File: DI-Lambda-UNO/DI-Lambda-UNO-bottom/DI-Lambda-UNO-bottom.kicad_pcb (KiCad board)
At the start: 2 copper layers, 38.2 x 128.1 mm, 49 parts, among them J10 CONN_02X05, J11 CONN_02X05, J15 CONN_01X06, J16 CONN_01X06, J17 CONN_02X03, J18 USB_OTG, J2 Conn_01X01, J3 CONN_02X05, J4 Conn_01X01, J6 CONN_02X05, J7 CONN_02X04, J8 CONN_02X04, Q1 AO3400, SW1 RESET, U2 USBLC6-2SC6, U3 ATMEGA32U4-MU, U4 3.3v LDO, U5 AP3032, Y1 8Mhz

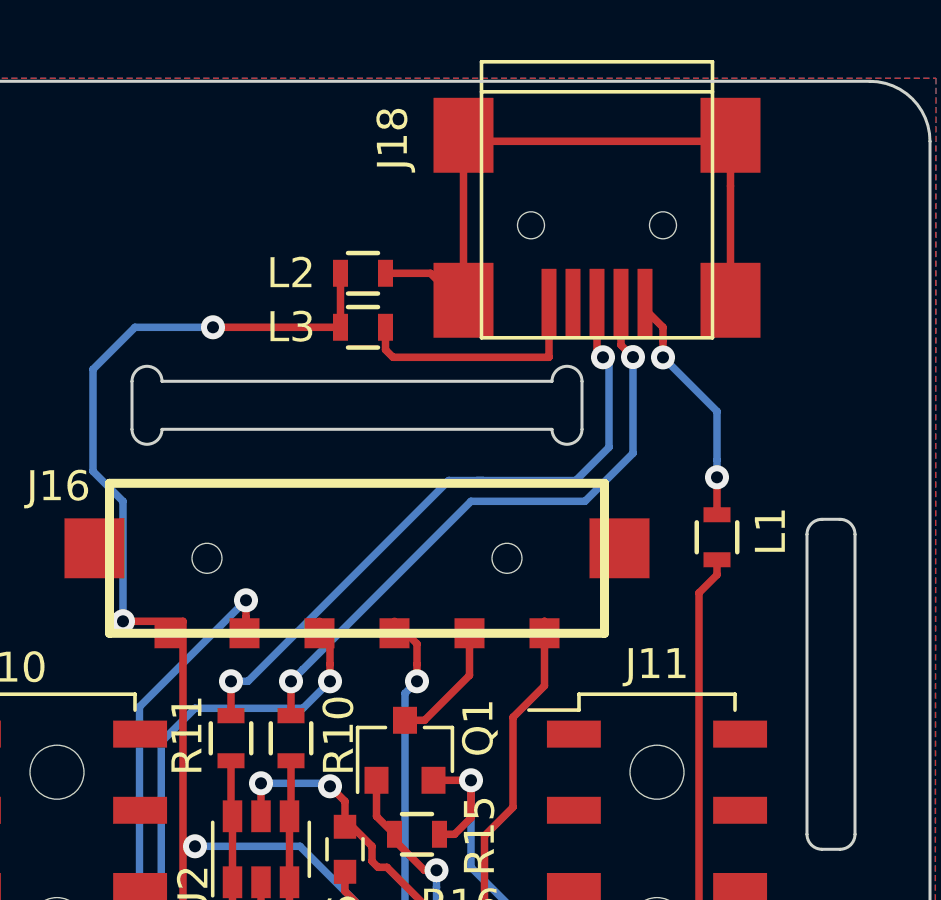
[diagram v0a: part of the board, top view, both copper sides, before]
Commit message: Use Micro-USB instead on Mini on the bottom plate
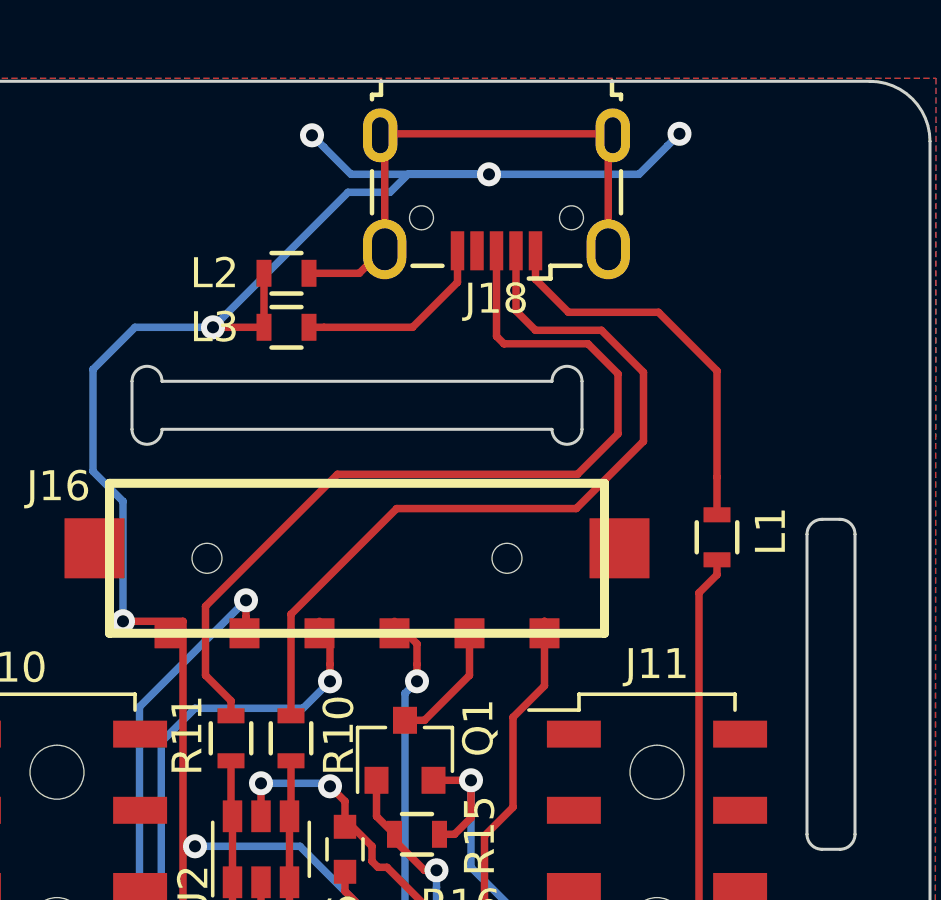
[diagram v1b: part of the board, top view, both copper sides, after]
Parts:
- J18: footprint Connectors:USB_Mini-B -> Connectors_USB:USB_Micro-B_Wuerth-629105150521
- moved J18 3.46 mm to (155.0, 39.8), turned to 180 degrees
- moved L2 2.55 mm to (148.0, 42.5)
- moved L3 2.55 mm to (148.0, 44.3)
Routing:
- net GND: track 196.8 -> 218.9 mm, vias 24 -> 27
- net Net-(J18-Pad3): track 22.1 -> 29.6 mm, vias 2 -> 0
- net Net-(J18-Pad2): track 20.9 -> 27.0 mm, vias 2 -> 0
- net Net-(J18-Pad1): track 7.84 -> 13.1 mm, vias 2 -> 0
- net Net-(J18-Pad6): track 23.0 -> 18.4 mm
- net Net-(J18-Pad5): track 7.90 -> 6.67 mm

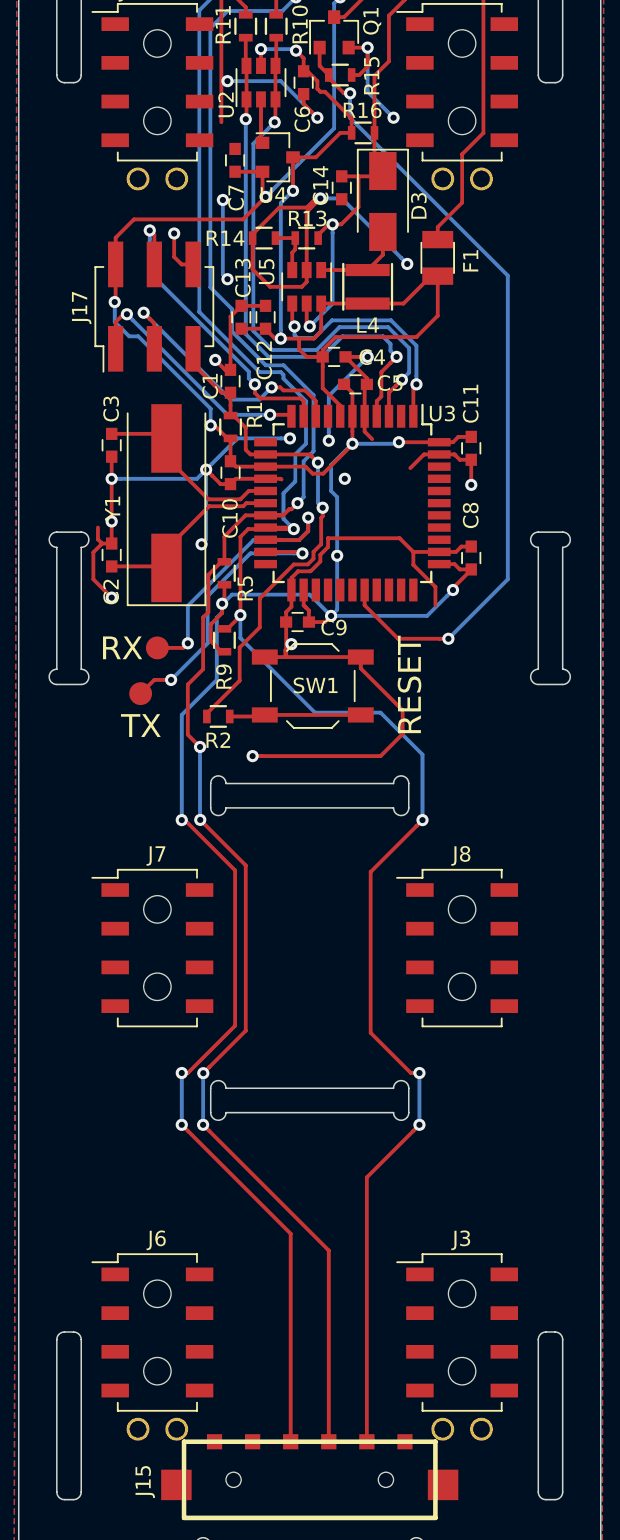
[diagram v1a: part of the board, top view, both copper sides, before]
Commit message: Change pinhole tab length to 15mm
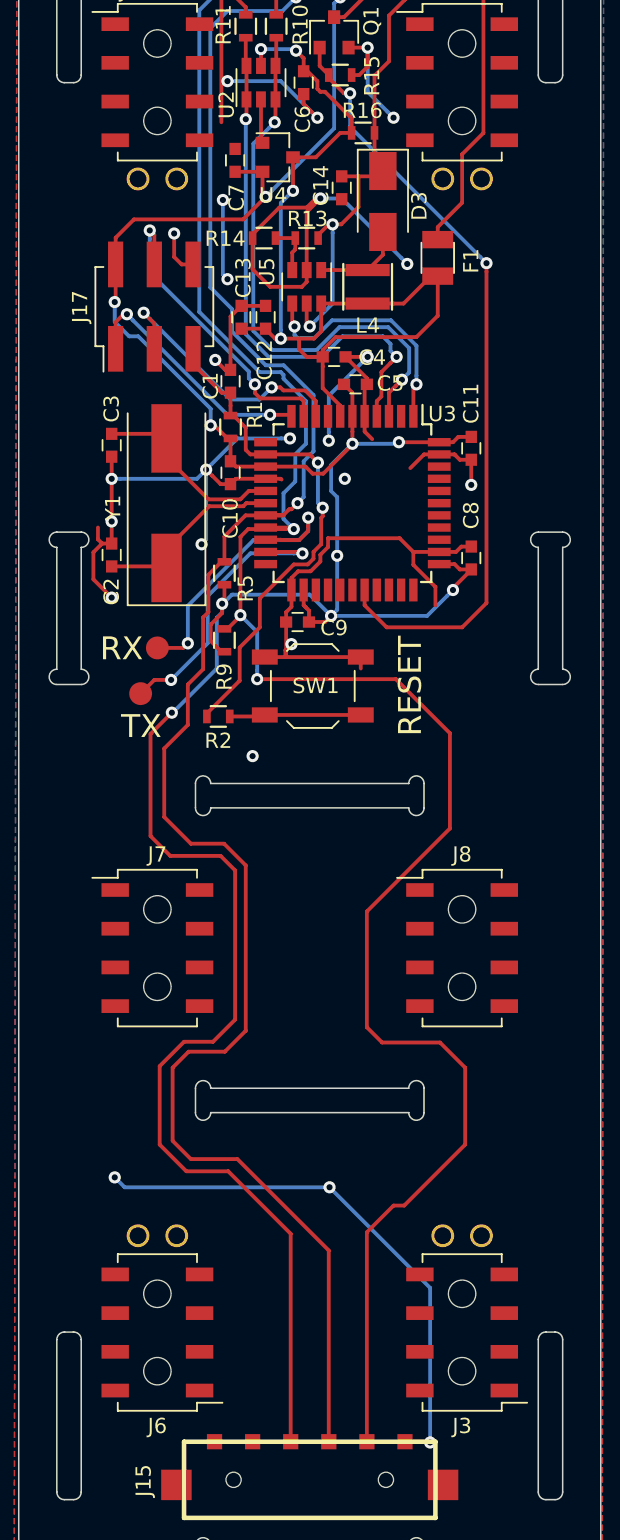
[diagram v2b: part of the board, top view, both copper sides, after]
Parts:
- turned J3 to 180 degrees
- turned J6 to 180 degrees
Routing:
- net GND: track 218.9 -> 238.5 mm, vias 27 -> 30
- net /SDA: track 123.1 -> 132.4 mm, vias 6 -> 4
- net /VCC: track 176.6 -> 183.8 mm, vias 13 -> 11
- net /SCL: track 117.7 -> 124.8 mm, vias 6 -> 2
- net /LED_PWM: track 53.2 -> 51.5 mm
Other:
- outline, holes or cut-outs redrawn

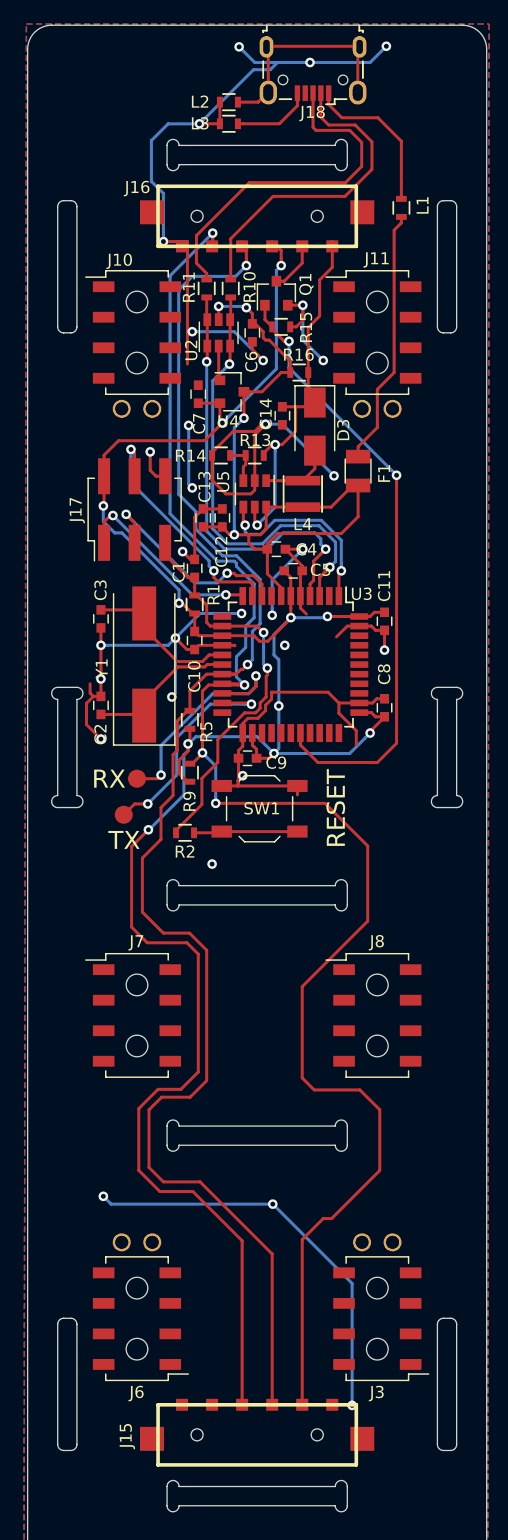
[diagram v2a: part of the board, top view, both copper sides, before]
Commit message: Update schematics to version 1.3
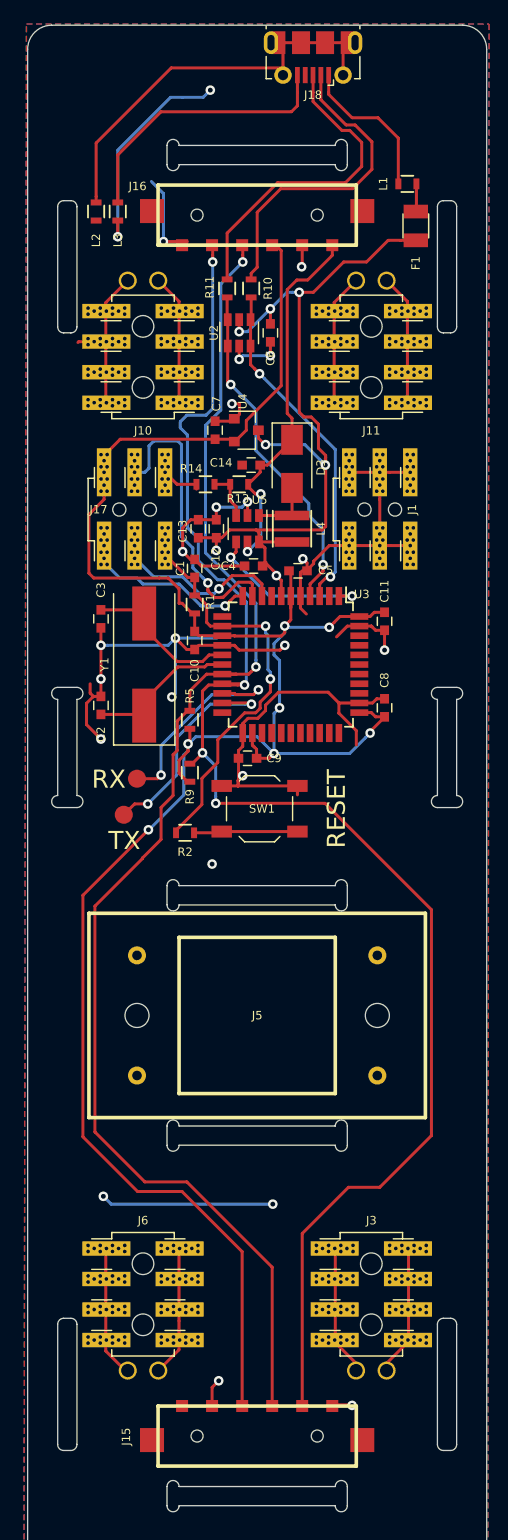
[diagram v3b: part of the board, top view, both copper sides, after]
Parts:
- removed J7, J8: CONN_02X04, Female_socket_pitch254_smt_through-board:Pin_Header_Straight_2x04_Pitch2.54mm_SMD
- removed Q1: AO3400, TO_SOT_Packages_SMD:SOT-23
- removed R15: 4.7k, Resistors_SMD:R_0603
- removed R16: DNP, Resistors_SMD:R_0603
- added J1: CONN_02X03, Female_socket_pitch254_smt_through-board:Pin_Header_Straight_2x03_Pitch2.54mm_SMD_wide, F.Cu at (160.6, 76.4)
- added J5: Conn_01x01, Cuvette-holder:Cuvette-holder, F.Cu at (150.4, 118.5)
- J10, J11, J3, J6: footprint Female_socket_pitch254_smt_through-board:Pin_Header_Straight_2x04_Pitch2.54mm_SMD_2THT -> Female_socket_pitch254_smt_through-board:Pin_Header_Straight_2x04_Pitch2.54mm_SMD_2THT_wide
- J17: footprint Pin_Headers:Pin_Header_Straight_2x03_Pitch2.54mm_SMD -> Female_socket_pitch254_smt_through-board:Pin_Header_Straight_2x03_Pitch2.54mm_SMD_wide
- J18: footprint Connectors_USB:USB_Micro-B_Wuerth-629105150521 -> Connectors_USB:USB_Micro-B_Molex-105017-0001
- moved F1 21.0 mm to (163.6, 52.8)
- moved L2 14.3 mm to (137.0, 51.6), turned to 270 degrees
- moved L3 11.8 mm to (138.8, 51.6), turned to 270 degrees
- moved C14 4.85 mm to (149.9, 72.7), turned to 180 degrees
- moved D3 3.64 mm to (153.3, 72.6)
- moved U4 3.42 mm to (149.5, 69.8)
- moved C7 3.31 mm to (146.9, 69.8)
- moved L4 3.04 mm to (153.3, 78.0)
- moved U5 2.96 mm to (149.6, 78.0)
- moved R13 2.73 mm to (148.9, 74.3)
- moved R14 2.73 mm to (146.1, 74.3)
- moved C4 2.36 mm to (150.1, 81.1), turned to 180 degrees
- moved J10 2.09 mm to (140.9, 63.7), turned to 180 degrees
- moved J11 2.09 mm to (159.9, 63.7), turned to 180 degrees
- moved J3 2.09 mm to (159.9, 141.7), turned to 0 degrees
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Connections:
- J10 pad 1: Net-(J10-Pad1) -> GND
- J10 pad 10: Net-(J10-Pad10) -> GND
- J10 pad 2: Net-(J10-Pad2) -> GND
- J10 pad 3: Net-(J10-Pad3) -> GND
- J10 pad 4: Net-(J10-Pad4) -> GND
- J10 pad 5: Net-(J10-Pad5) -> GND
- J10 pad 6: Net-(J10-Pad6) -> GND
- J10 pad 7: Net-(J10-Pad7) -> GND
- J10 pad 8: Net-(J10-Pad8) -> GND
- J10 pad 9: Net-(J10-Pad9) -> GND
- J11 pad 1: Net-(J11-Pad1) -> GND
- J11 pad 10: Net-(J11-Pad10) -> GND
- J11 pad 2: Net-(J11-Pad2) -> GND
- J11 pad 3: Net-(J11-Pad3) -> GND
- J11 pad 4: Net-(J11-Pad4) -> GND
- J11 pad 5: Net-(J11-Pad5) -> GND
- J11 pad 6: Net-(J11-Pad6) -> GND
- J11 pad 7: Net-(J11-Pad7) -> GND
- J11 pad 8: Net-(J11-Pad8) -> GND
- J11 pad 9: Net-(J11-Pad9) -> GND
- J15 pad 5: Net-(J15-Pad5) -> GND
- J16 pad 5: /GLED -> GND
- J3 pad 1: Net-(J3-Pad1) -> GND
- J3 pad 10: Net-(J3-Pad10) -> GND
- J3 pad 2: Net-(J3-Pad2) -> GND
- J3 pad 3: Net-(J3-Pad3) -> GND
- J3 pad 4: Net-(J3-Pad4) -> GND
- J3 pad 5: Net-(J3-Pad5) -> GND
- J3 pad 6: Net-(J3-Pad6) -> GND
- J3 pad 7: Net-(J3-Pad7) -> GND
- J3 pad 8: Net-(J3-Pad8) -> GND
- J3 pad 9: Net-(J3-Pad9) -> GND
- J6 pad 1: Net-(J6-Pad1) -> GND
- J6 pad 10: Net-(J6-Pad10) -> GND
- J6 pad 2: Net-(J6-Pad2) -> GND
- J6 pad 3: Net-(J6-Pad3) -> GND
- J6 pad 4: Net-(J6-Pad4) -> GND
- J6 pad 5: Net-(J6-Pad5) -> GND
- J6 pad 6: Net-(J6-Pad6) -> GND
- J6 pad 7: Net-(J6-Pad7) -> GND
- J6 pad 8: Net-(J6-Pad8) -> GND
- J6 pad 9: Net-(J6-Pad9) -> GND
- U3 pad 29: /LED_PWM -> Net-(U3-Pad29)
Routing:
- net /LED_PWM: track 51.5 -> 0.00 mm, vias 2 -> 0
- net GND: track 238.5 -> 261.7 mm, vias 30 -> 24
- net Net-(F1-Pad2): track 21.4 -> 2.32 mm
- net Net-(J18-Pad6): track 18.4 -> 36.7 mm
- net Net-(J18-Pad5): track 6.67 -> 23.1 mm
- net Net-(R10-Pad1): track 36.8 -> 28.5 mm
- net /SCL: track 124.8 -> 117.1 mm
- net /VBUS: track 63.0 -> 70.5 mm, vias 4 -> 7
- net Net-(R11-Pad1): track 35.8 -> 28.6 mm
- net /MOSI: track 20.3 -> 26.7 mm, vias 2 -> 1
- net /SDA: track 132.4 -> 127.5 mm
- net /GLED: track 4.27 -> 0.00 mm
- net /SCK: track 18.9 -> 14.7 mm, vias 2 -> 1
- net Net-(J18-Pad3): track 29.6 -> 27.0 mm
- net /BOOST_CTRL: track 16.1 -> 14.0 mm
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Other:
- board text added: "DI-Lambda UNO v1.3"
- board text removed: "DI-Lambda UNO v1.1"

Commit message: Version 1.5 redesign WIP
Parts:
- removed J10, J11: CONN_02X05, Female_socket_pitch254_smt_through-board:Pin_Header_Straight_2x04_Pitch2.54mm_SMD_2THT_wide
- added J7: Conn_02x03_Odd_Even, Board_grooves:Pocket_1.6mm_10mm_2cap_6pads_short_vias, B.Cu at (134.6, 96.2)
- added J8: Conn_02x04_Odd_Even, Board_grooves:Pocket_1.6mm_10mm_no_cap_8pads_short_vias, B.Cu at (134.6, 149.2)
- added J9: Conn_02x04_Odd_Even, Board_grooves:Pocket_1.6mm_10mm_no_cap_8pads_short_vias, B.Cu at (166.2, 56.2)
- added MK1: Mounting_Hole, DI-Lambda-module-tabs:Slot_pinhole, F.Cu at (150.4, 128.5)
- added MK2: Mounting_Hole, DI-Lambda-module-tabs:Slot_LED, F.Cu at (150.4, 46.9)
- added MK3: Mounting_Hole, DI-Lambda-module-tabs:Slot_pinhole, F.Cu at (150.4, 108.5)
- added MK4: Mounting_Hole, DI-Lambda-module-tabs:Slot_sensor, F.Cu at (150.4, 158.5)
- added Q1: Q_NMOS_GSD, Package_TO_SOT_SMD:SOT-23, F.Cu at (154.4, 58.8)
- added R3: 4.7k, Resistor_SMD:R_0603_1608Metric, F.Cu at (154.4, 61.8)
- C1, C10, C11, C12, C13, C14, C2, C3, C4, C5, C6, C7, C8, C9: footprint Capacitors_SMD:C_0603 -> Capacitor_SMD:C_0603_1608Metric
- J1: value CONN_02X03 -> Conn_02x04_Odd_Even; footprint Female_socket_pitch254_smt_through-board:Pin_Header_Straight_2x03_Pitch2.54mm_SMD_wide -> Board_grooves:Pocket_1.6mm_10mm_no_cap_8pads_short_vias; moved to B.Cu
- J3: value CONN_02X05 -> Conn_02x04_Odd_Even; footprint Female_socket_pitch254_smt_through-board:Pin_Header_Straight_2x04_Pitch2.54mm_SMD_2THT_wide -> Board_grooves:Pocket_1.6mm_10mm_no_cap_8pads_short_vias; moved to B.Cu
- J6: value CONN_02X05 -> Conn_02x03_Odd_Even; footprint Female_socket_pitch254_smt_through-board:Pin_Header_Straight_2x04_Pitch2.54mm_SMD_2THT_wide -> Board_grooves:Pocket_1.6mm_10mm_2cap_6pads_short_vias; moved to B.Cu
- L1, L2, L3: footprint Resistors_SMD:R_0603 -> Inductor_SMD:L_0603_1608Metric
- R1, R10, R11, R13, R14, R2, R5, R9: footprint Resistors_SMD:R_0603 -> Resistor_SMD:R_0603_1608Metric
- moved J6 52.1 mm to (166.2, 96.2), turned to 270 degrees
- moved J1 32.9 mm to (134.6, 56.2), turned to 270 degrees
- moved J3 9.79 mm to (166.2, 149.2), turned to 270 degrees
- moved L2 7.12 mm to (139.1, 58.4)
- moved L3 7.12 mm to (140.9, 58.4)
- moved F1 6.44 mm to (160.2, 58.3), turned to 0 degrees
- moved C2 2.40 mm to (137.4, 90.3)
- moved L1 2.00 mm to (162.1, 51.1), turned to 90 degrees
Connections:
- J1 pad 1: GND -> Net-(J1-Pad1)
- J1 pad 2: GND -> Net-(J1-Pad2)
- J1 pad 3: GND -> Net-(J1-Pad3)
- J1 pad 4: GND -> Net-(J1-Pad4)
- J1 pad 5: GND -> Net-(J1-Pad5)
- J1 pad 6: GND -> Net-(J1-Pad6)
- J15 pad 1: GND -> /VCC
- J15 pad 4: /VCC -> GND
- J16 pad 1: GND -> /VCC
- J16 pad 4: /VCC -> GND
- J16 pad 5: GND -> /GLED
- J3 pad 1: GND -> Net-(J3-Pad1)
- J3 pad 2: GND -> Net-(J3-Pad2)
- J3 pad 3: GND -> Net-(J3-Pad3)
- J3 pad 4: GND -> Net-(J3-Pad4)
- J3 pad 5: GND -> Net-(J3-Pad5)
- J3 pad 6: GND -> Net-(J3-Pad6)
- J3 pad 7: GND -> Net-(J3-Pad7)
- J3 pad 8: GND -> Net-(J3-Pad8)
- J6 pad 1: GND -> Net-(J6-Pad1)
- J6 pad 2: GND -> Net-(J6-Pad2)
- J6 pad 3: GND -> Net-(J6-Pad3)
- J6 pad 4: GND -> Net-(J6-Pad4)
- J6 pad 5: GND -> Net-(J6-Pad5)
- J6 pad 6: GND -> Net-(J6-Pad6)
- U3 pad 29: Net-(U3-Pad29) -> /LED_PWM
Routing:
- net GND: track 261.7 -> 121.9 mm, vias 24 -> 22
- net /LED_PWM: track 0.00 -> 44.4 mm, vias 0 -> 2
- net /VCC: track 185.7 -> 195.6 mm
- net Net-(J18-Pad5): track 23.1 -> 30.0 mm
- net /VBUS: track 70.5 -> 64.2 mm
- net Net-(J18-Pad6): track 36.7 -> 42.6 mm
- net Net-(F1-Pad2): track 2.32 -> 6.69 mm
- net /GLED: track 0.00 -> 3.50 mm
- net /SDA: track 127.5 -> 124.9 mm
- net /VLED: track 32.1 -> 31.4 mm
- net Net-(C2-Pad1): track 12.6 -> 13.3 mm
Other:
- board size 38.2 x 128.1 mm -> 118.4 x 128.1 mm
- board text added: "DI-Lambda UNO v1.5"
- board text removed: "DI-Lambda UNO v1.3"
